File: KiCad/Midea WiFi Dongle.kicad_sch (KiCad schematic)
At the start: 18 parts, among them J1 USB_A, Q1 BSS138, Q2 BSS138, SW1 SW_Push, SW2 SW_Push, U1 AMS1117-3.3, U2 WT0132C6-S5

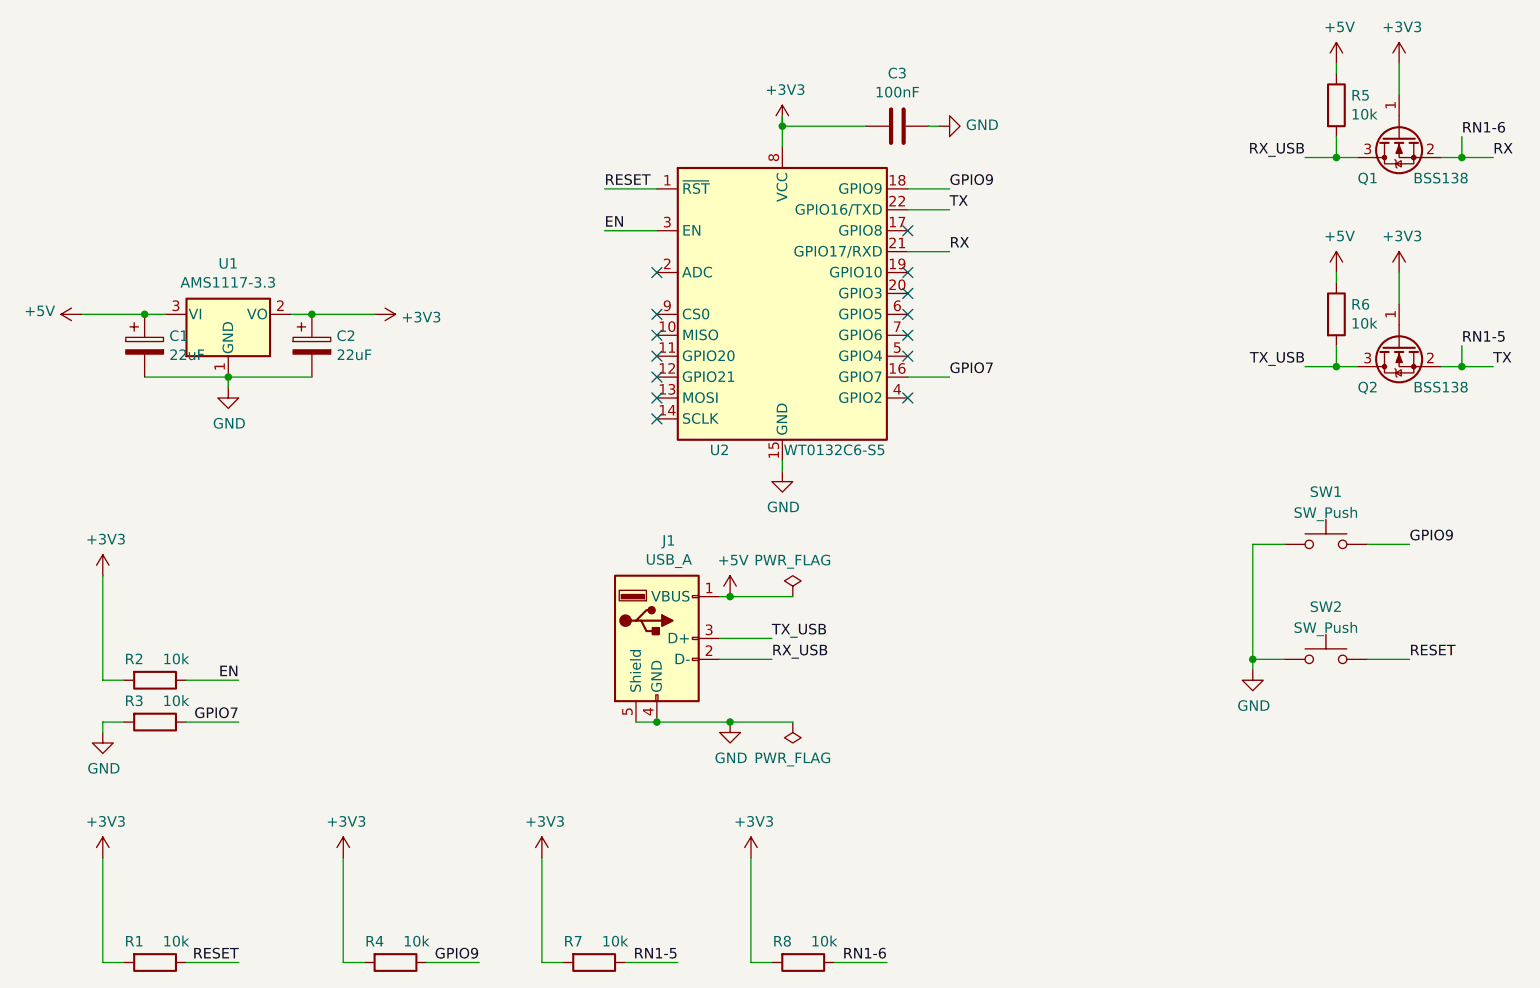
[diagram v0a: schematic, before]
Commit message: updated 3D model, I have to update the 3D printing model too.
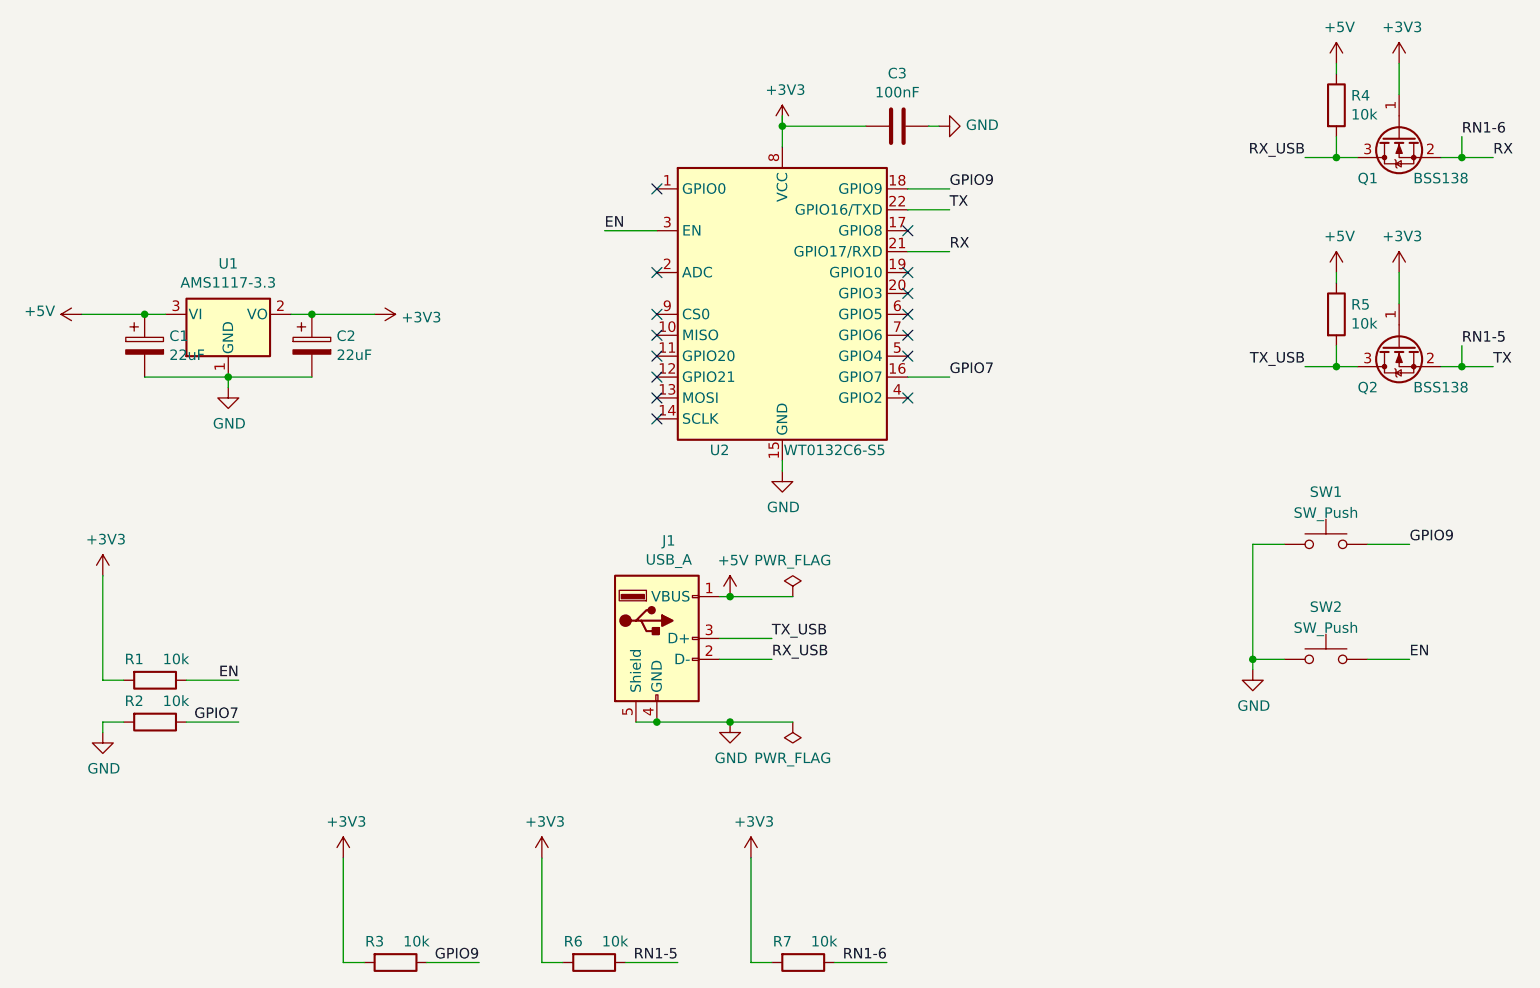
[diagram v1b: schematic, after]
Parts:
- removed R1: 10k, Resistor_SMD:R_0402_1005Metric_Pad0.72x0.64mm_HandSolder, symbol Device:R
- renumbered R2 to R1, R3 to R2, R4 to R3, R5 to R4, R6 to R5, R7 to R6, R8 to R7
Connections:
- net EN: now also SW2.2
- net RESET: no longer names the net of U2.1 (GPIO0)
- net RESET: no longer SW2.2
- no-connect marks 14 -> 15
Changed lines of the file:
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@@
 	)
 	(no_connect
+		(at 125.73 68.58)
+	)
+	(no_connect
 		(at 156.21 73.66)
 	)
@@
 	(wire
 		(pts
-			(xy 58.42 149.86) (xy 58.42 162.56)
-		)
-		(stroke
-			(width 0)
-			(type default)
-		)
-	)
-	(wire
-		(pts
 			(xy 73.66 91.44) (xy 73.66 92.71)
 		)
@@
 	(wire
 		(pts
-			(xy 58.42 162.56) (xy 60.96 162.56)
-		)
-		(stroke
-			(width 0)
-			(type default)
-		)
-	)
-	(wire
-		(pts
 			(xy 223.52 64.77) (xy 227.33 64.77)
 		)
@@
 	(wire
 		(pts
-			(xy 68.58 162.56) (xy 74.93 162.56)
-		)
-		(stroke
-			(width 0)
-			(type default)
-		)
-	)
-	(wire
-		(pts
 			(xy 156.21 71.12) (xy 161.29 71.12)
 		)
@@
 	(wire
 		(pts
-			(xy 125.73 68.58) (xy 119.38 68.58)
-		)
-		(stroke
-			(width 0)
-			(type default)
-		)
-	)
-	(wire
-		(pts
 			(xy 87.63 149.86) (xy 87.63 162.56)
 		)
@@
 		)
 	)
-	(label "RESET"
-		(at 74.93 162.56 180)
-		(effects
-			(font
-				(size 1.27 1.27)
-			)
-			(justify right bottom)
-		)
-	)
 	(label "GPIO7"
 		(at 74.93 133.35 180)
@@
 		)
 	)
-	(label "RESET"
+	(label "EN"
 		(at 217.17 125.73 0)
 		(effects
@@
 		)
 	)
-	(label "RESET"
-		(at 119.38 68.58 0)
-		(effects
-			(font
-				(size 1.27 1.27)
-			)
-			(justify left bottom)
-		)
-	)
 	(label "RN1-5"
 		(at 128.27 162.56 180)
@@
 		(on_board yes)
 		(dnp no)
-		(property "Reference" "R5"
+		(property "Reference" "R4"
 			(at 210.058 57.2516 0)
 			(effects
@@
 			(project "Midea WiFi Dongle"
 				(path "/ee1d3c30-6791-41bb-a985-8c603430de03"
-					(reference "R5")
+					(reference "R4")
 					(unit 1)
 				)
@@
 		(on_board yes)
 		(dnp no)
-		(property "Reference" "R6"
+		(property "Reference" "R5"
 			(at 210.058 82.6516 0)
 			(effects
@@
 			(project "Midea WiFi Dongle"
 				(path "/ee1d3c30-6791-41bb-a985-8c603430de03"
-					(reference "R6")
+					(reference "R5")
 					(unit 1)
 				)
@@
 		(on_board yes)
 		(dnp no)
-		(property "Reference" "R2"
+		(property "Reference" "R1"
 			(at 62.23 125.73 90)
 			(effects
@@
 			(project "Midea WiFi Dongle"
 				(path "/ee1d3c30-6791-41bb-a985-8c603430de03"
-					(reference "R2")
+					(reference "R1")
 					(unit 1)
 				)
@@
 		(on_board yes)
 		(dnp no)
-		(property "Reference" "R3"
+		(property "Reference" "R2"
 			(at 62.23 130.81 90)
 			(effects
@@
 			(project "Midea WiFi Dongle"
 				(path "/ee1d3c30-6791-41bb-a985-8c603430de03"
-					(reference "R3")
+					(reference "R2")
 					(unit 1)
 				)
@@
 		(on_board yes)
 		(dnp no)
-		(property "Reference" "R8"
+		(property "Reference" "R7"
 			(at 140.97 160.02 90)
 			(effects
@@
 			(project "Midea WiFi Dongle"
 				(path "/ee1d3c30-6791-41bb-a985-8c603430de03"
-					(reference "R8")
+					(reference "R7")
 					(unit 1)
 				)
@@
 		(on_board yes)
 		(dnp no)
-		(property "Reference" "R7"
+		(property "Reference" "R6"
 			(at 115.57 160.02 90)
 			(effects
@@
 			(project "Midea WiFi Dongle"
 				(path "/ee1d3c30-6791-41bb-a985-8c603430de03"
-					(reference "R7")
+					(reference "R6")
 					(unit 1)
 				)
@@
 	)
 	(symbol
-		(lib_id "Midea WiFi Dongle-rescue:+3.3V-power")
-		(at 58.42 149.86 0)
-		(unit 1)
-		(exclude_from_sim no)
-		(in_bom yes)
-		(on_board yes)
-		(dnp no)
-		(property "Reference" "#PWR02"
-			(at 58.42 153.67 0)
-			(effects
-				(font
-					(size 1.27 1.27)
-				)
-				(hide yes)
-			)
-		)
-		(property "Value" "+3V3"
-			(at 58.801 145.4658 0)
-			(effects
-				(font
-					(size 1.27 1.27)
-				)
-			)
-		)
-		(property "Footprint" ""
-			(at 58.42 149.86 0)
-			(effects
-				(font
-					(size 1.27 1.27)
-				)
-				(hide yes)
-			)
-		)
-		(property "Datasheet" ""
-			(at 58.42 149.86 0)
-			(effects
-				(font
-					(size 1.27 1.27)
-				)
-				(hide yes)
-			)
-		)
-		(property "Description" ""
-			(at 58.42 149.86 0)
-			(effects
-				(font
-					(size 1.27 1.27)
-				)
-				(hide yes)
-			)
-		)
-		(pin "1"
-		)
-		(instances
-			(project "Midea WiFi Dongle"
-				(path "/ee1d3c30-6791-41bb-a985-8c603430de03"
-					(reference "#PWR02")
-					(unit 1)
-				)
-			)
-		)
-	)
-	(symbol
-		(lib_id "Device:R")
-		(at 64.77 162.56 270)
-		(unit 1)
-		(exclude_from_sim no)
-		(in_bom yes)
-		(on_board yes)
-		(dnp no)
-		(property "Reference" "R1"
-			(at 62.23 160.02 90)
-			(effects
-				(font
-					(size 1.27 1.27)
-				)
-			)
-		)
-		(property "Value" "10k"
-			(at 67.31 160.02 90)
-			(effects
-				(font
-					(size 1.27 1.27)
-				)
-			)
-		)
-		(property "Footprint" "Resistor_SMD:R_0402_1005Metric_Pad0.72x0.64mm_HandSolder"
-			(at 64.77 160.782 90)
-			(effects
-				(font
-					(size 1.27 1.27)
-				)
-				(hide yes)
-			)
-		)
-		(property "Datasheet" "~"
-			(at 64.77 162.56 0)
-			(effects
-				(font
-					(size 1.27 1.27)
-				)
-				(hide yes)
-			)
-		)
-		(property "Description" ""
-			(at 64.77 162.56 0)
-			(effects
-				(font
-					(size 1.27 1.27)
-				)
-				(hide yes)
-			)
-		)
-		(property "LCSC" "C25744"
-			(at 64.77 162.56 90)
-			(effects
-				(font
-					(size 1.27 1.27)
-				)
-				(hide yes)
-			)
-		)
-		(pin "1"
-		)
-		(pin "2"
-		)
-		(instances
-			(project "Midea WiFi Dongle"
-				(path "/ee1d3c30-6791-41bb-a985-8c603430de03"
-					(reference "R1")
-					(unit 1)
-				)
-			)
-		)
-	)
-	(symbol
 		(lib_id "Switch:SW_Push")
 		(at 207.01 125.73 0)
@@
 		(on_board yes)
 		(dnp no)
-		(property "Reference" "R4"
+		(property "Reference" "R3"
 			(at 91.44 160.02 90)
 			(effects
@@
 			(project "Midea WiFi Dongle"
 				(path "/ee1d3c30-6791-41bb-a985-8c603430de03"
-					(reference "R4")
+					(reference "R3")
 					(unit 1)
 				)
